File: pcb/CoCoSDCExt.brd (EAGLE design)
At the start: 101.6 x 47 mm, 49 parts, among them IC1 AM29F040J, IC10 YAC512-M, IC14 TL974, IC15 TL974, IC2 XC9572XLVQG64, IC3 AS6C4008SIN, IC9 YMF262-M, X1 EXPANSION_PORT_COCO, X2 EXPANSION_PORT_COCOS

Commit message: nearly routed
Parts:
- moved C20 12.3 mm to (23.2, 26.0)
- moved C2.2 11.9 mm to (16.5, 14.9), turned to 270 degrees
- moved JP1 7.62 mm to (-16.2, 19.7), turned to 270 degrees
- moved TCK 4.51 mm to (16.5, 19.4)
- moved TDI 4.24 mm to (14.6, 17.5)
- moved C2.4 3.17 mm to (17.5, 21.6)
- moved GND 2.73 mm to (14.6, 21.3)
- moved IC2 2.62 mm to (12.7, 18.4), turned to 45 degrees
- moved TMS 2.25 mm to (12.7, 19.4)
- moved C2.1 2.01 mm to (9.84, 21.9), turned to 90 degrees
- moved C2.3 1.71 mm to (9.84, 15.9), turned to 270 degrees
- moved TDO 1.62 mm to (12.7, 23.2)
- moved X2 1.27 mm to (0.00, 30.5)
- moved 3V3 0.45 mm to (10.8, 21.3)
- moved R16 0.32 mm to (47.3, 14.3)
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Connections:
- removed net !CE_SN: IC2.2
- removed net !CE_YM: IC2.58
- removed net !RESET_YM: IC2.59
- removed net !WE_SN: IC2.5
- removed net A0_YM: IC2.57
- removed net BD0: IC2.1
- removed net BD1: IC2.4
- removed net BD2: IC2.6
- removed net BD3: IC2.8
- removed net BD4: IC2.12
- removed net BD5: IC2.13
- removed net BD6: IC2.11
- removed net BD7: IC2.9
- removed net CH2: IC2.60
- removed net CLK_SN: IC2.10
- removed net CLK_YM: IC2.56
- removed net READY: IC2.7
- removed net VCC: IC3.32
- new net !CE_FLASH: IC1.22, IC2.2
- new net !CE_RAM: IC2.47, IC3.22
- net !CTS: now also IC2.20; no longer IC1.24
- net !RESET: now also IC2.4; no longer IC2.16
- net !SCS: now also IC2.23; no longer IC2.48
- net !SLENB: now also IC2.25; no longer IC2.50
- net !WE: now also IC2.51, IC3.29; no longer IC2.42
- net +5V: now also IC3.32
- net A0: now also IC2.5, IC3.5; no longer IC2.32
- net A1: now also IC2.1, IC3.6; no longer IC2.35
- net A10: now also IC2.49, IC3.31
- net A11: now also IC2.50, IC3.30
- net A12: now also IC2.17, IC3.4
- net A13: now also IC2.59, IC3.1; no longer IC2.33
- net A14: now also IC2.24; no longer IC2.49
- net A15: now also IC2.27; no longer IC2.34
- net A2: now also IC2.64, IC3.7; no longer IC2.38
- net A3: now also IC2.63, IC3.8; no longer IC2.40
- net A4: now also IC2.62, IC3.9; no longer IC2.43
- net A5: now also IC2.61, IC3.10; no longer IC2.45
- net A6: now also IC2.60, IC3.11
- net A7: now also IC2.58, IC3.12
- net A8: now also IC2.18, IC3.27
- net A9: now also IC2.52, IC3.28
- net BA14: now also IC2.57, IC3.26; no longer IC2.36
- net BA15: now also IC2.19, IC3.3; no longer IC2.47
- net BA16: now also IC2.22, IC3.2; no longer IC2.46
- net BA17: now also IC2.56, IC3.25; no longer IC2.39
- net BA18: now also IC2.48, IC3.23; no longer IC2.44
- net D0: now also IC2.13, IC3.17; no longer IC2.18
- net D1: now also IC2.12, IC3.15; no longer IC2.19
- net D2: now also IC2.11, IC3.18; no longer IC2.20
- net D3: now also IC2.10, IC3.14; no longer IC2.22
- net D4: now also IC2.9, IC3.19; no longer IC2.23
- net D5: now also IC2.8, IC3.13; no longer IC2.24
- net D6: now also IC2.7, IC3.20; no longer IC2.25
- net D7: now also IC2.6, IC3.21; no longer IC2.27
- net E: now also IC2.15; no longer IC2.17
- net GND: now also IC1.24, IC3.24; no longer IC1.22
- net R/!W: now also IC2.16; no longer IC2.31
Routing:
- net BA15: track 0.00 -> 93.9 mm, vias 0 -> 4
- net BA16: track 0.00 -> 92.9 mm, vias 0 -> 4
- net A0: track 25.0 -> 112.1 mm, vias 2 -> 5
- net A1: track 24.4 -> 110.8 mm, vias 0 -> 3
- net A13: track 25.5 -> 110.6 mm, vias 2 -> 5
- net D5: track 25.0 -> 109.5 mm, vias 2 -> 6
- net A12: track 25.0 -> 109.5 mm, vias 2 -> 5
- net A2: track 25.0 -> 106.9 mm, vias 2 -> 5
- net A3: track 24.4 -> 105.8 mm, vias 0 -> 3
- net A4: track 25.0 -> 104.8 mm, vias 2 -> 5
- net A5: track 24.4 -> 103.4 mm, vias 0 -> 3
- net A6: track 25.0 -> 103.8 mm, vias 2 -> 5
- net A7: track 24.4 -> 102.3 mm, vias 0 -> 3
- net D6: track 24.4 -> 96.1 mm, vias 0 -> 3
- net A8: track 25.0 -> 91.4 mm, vias 2 -> 6
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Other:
- board size 101.6 x 47 mm -> 101.6 x 47.3 mm

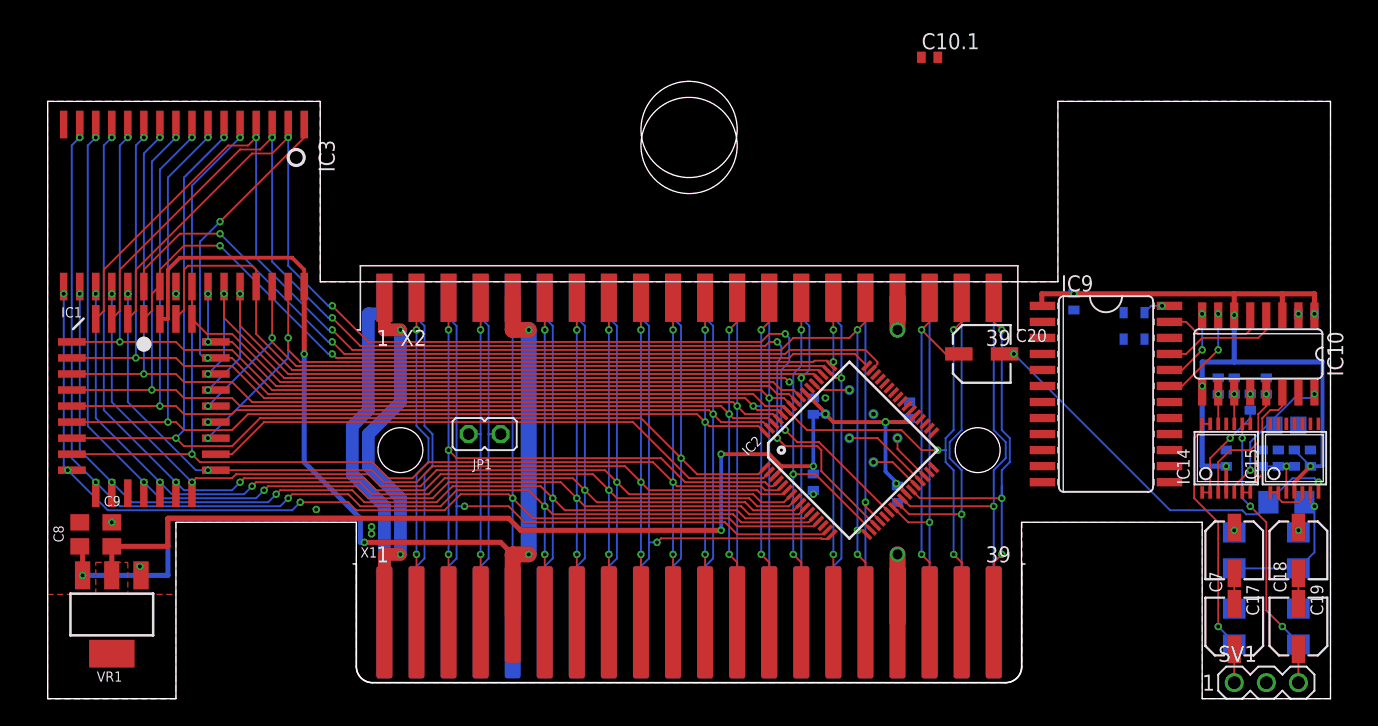
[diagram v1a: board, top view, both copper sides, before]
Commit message: fully routed
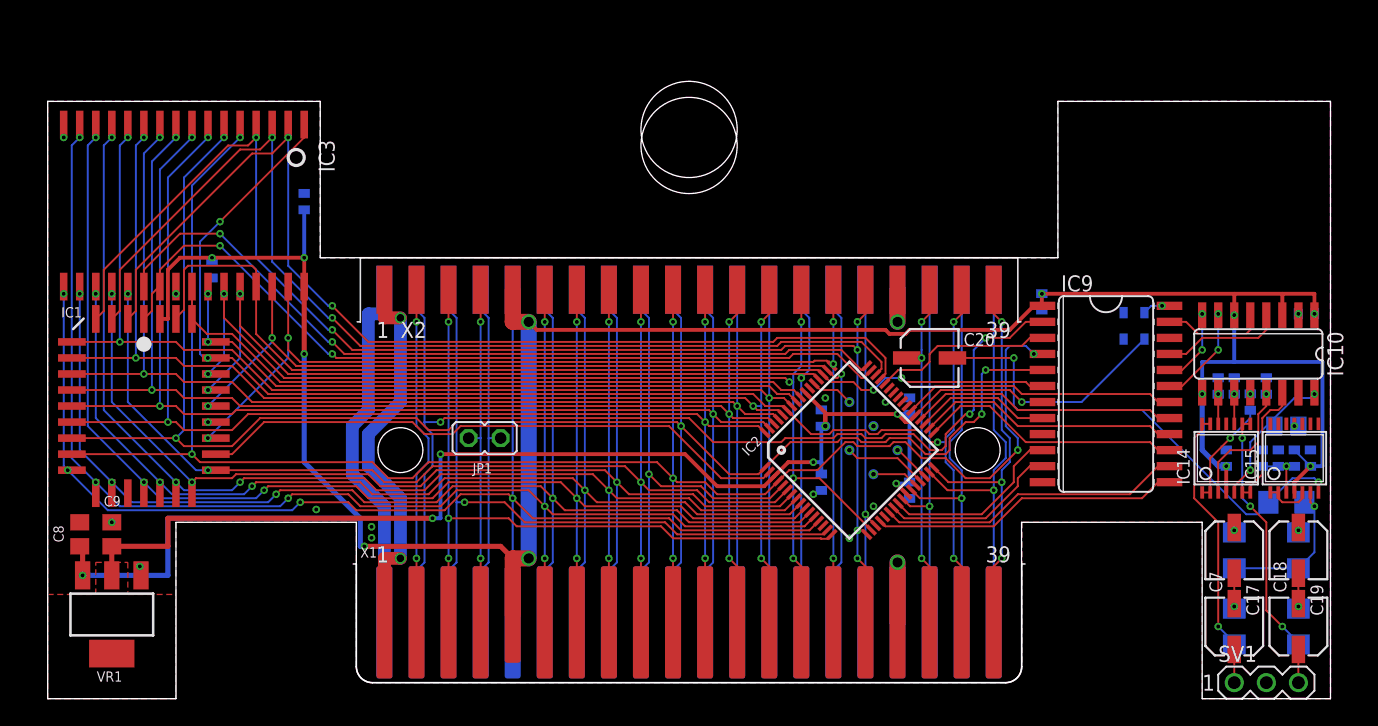
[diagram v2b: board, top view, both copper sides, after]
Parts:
- added C3.1: .1, resistor:C0402
- moved C1.1 86.7 mm to (-37.8, 32.7), turned to 270 degrees
- moved C10.1 36.1 mm to (48.9, 29.2), flipped to the bottom
- moved C20 4.14 mm to (19.1, 25.7)
- moved C9.1 2.54 mm to (27.9, 30.2)
- moved C2.1 1.14 mm to (10.5, 21.0)
- moved C2.2 1.00 mm to (17.5, 15.2)
- moved 3V3 0.95 mm to (10.8, 20.3)
- moved GND 0.95 mm to (14.6, 20.3)
- moved TCK 0.95 mm to (16.5, 18.4)
- moved TMS 0.95 mm to (12.7, 18.4)
- moved TDI 0.95 mm to (14.6, 16.5)
- moved TDO 0.95 mm to (12.7, 22.2)
- moved C2.3 0.63 mm to (10.5, 15.9)
- moved X2 0.63 mm to (0.00, 31.1)
- moved C2.4 0.32 mm to (17.5, 21.9)
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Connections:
- removed net !IRQ_AUDIO: IC9.2
- removed net !OE: IC9.7
- removed net AB0: IC9.4
- removed net AB1: IC9.5
- net !CE_RAM: now also IC2.48; no longer IC2.47
- net !CE_YMF262: now also IC2.35
- net !CTS: now also IC2.19; no longer IC2.20
- net !NMI: now also IC9.2
- net !RESET: now also IC2.16; no longer IC2.4
- net !RESET_AUDIO: now also IC2.44
- net !SCS: now also IC2.25; no longer IC2.23
- net !SLENB: now also IC2.31; no longer IC2.25
- net +5V: now also C3.1.1
- net A0: now also IC2.4, IC9.4; no longer IC2.5
- net A1: now also IC9.5
- net A14: now also IC2.27; no longer IC2.24
- net A15: now also IC2.32; no longer IC2.27
- net BA15: now also IC2.46; no longer IC2.19
- net BA16: now also IC2.45; no longer IC2.22
- net BA18: now also IC2.47; no longer IC2.48
- net DB0: now also IC2.24
- net DB1: now also IC2.23
- net DB2: now also IC2.20
- net DB3: now also IC2.22
- net DB4: now also IC2.33
- net DB5: now also IC2.34
- net DB6: now also IC2.36
- net DB7: now also IC2.38
- net GND: now also C3.1.2, IC9.7
- net R/!W: now also IC2.5; no longer IC2.16
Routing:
- net !NMI: track 26.8 -> 85.9 mm, vias 0 -> 3
- net +5V: track 176.9 -> 223.3 mm, vias 11 -> 13
- net A0: track 112.1 -> 147.0 mm, vias 5 -> 7
- net A1: track 110.8 -> 140.8 mm, vias 3 -> 5
- net DB2: track 0.00 -> 24.5 mm
- net DB3: track 0.00 -> 24.4 mm
- net DB7: track 0.00 -> 21.8 mm
- net DB6: track 0.00 -> 21.3 mm
- net +3V3: track 92.5 -> 113.8 mm, vias 6 -> 7
- net DB4: track 0.00 -> 21.0 mm
- net DB5: track 0.00 -> 20.9 mm
- net !WE: track 63.2 -> 81.7 mm, vias 0 -> 2
- net DB0: track 0.00 -> 14.6 mm
- net !RESET_AUDIO: track 0.00 -> 14.4 mm
- net DB1: track 0.00 -> 14.2 mm
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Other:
- outline, holes or cut-outs redrawn

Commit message: Added SN76489AN
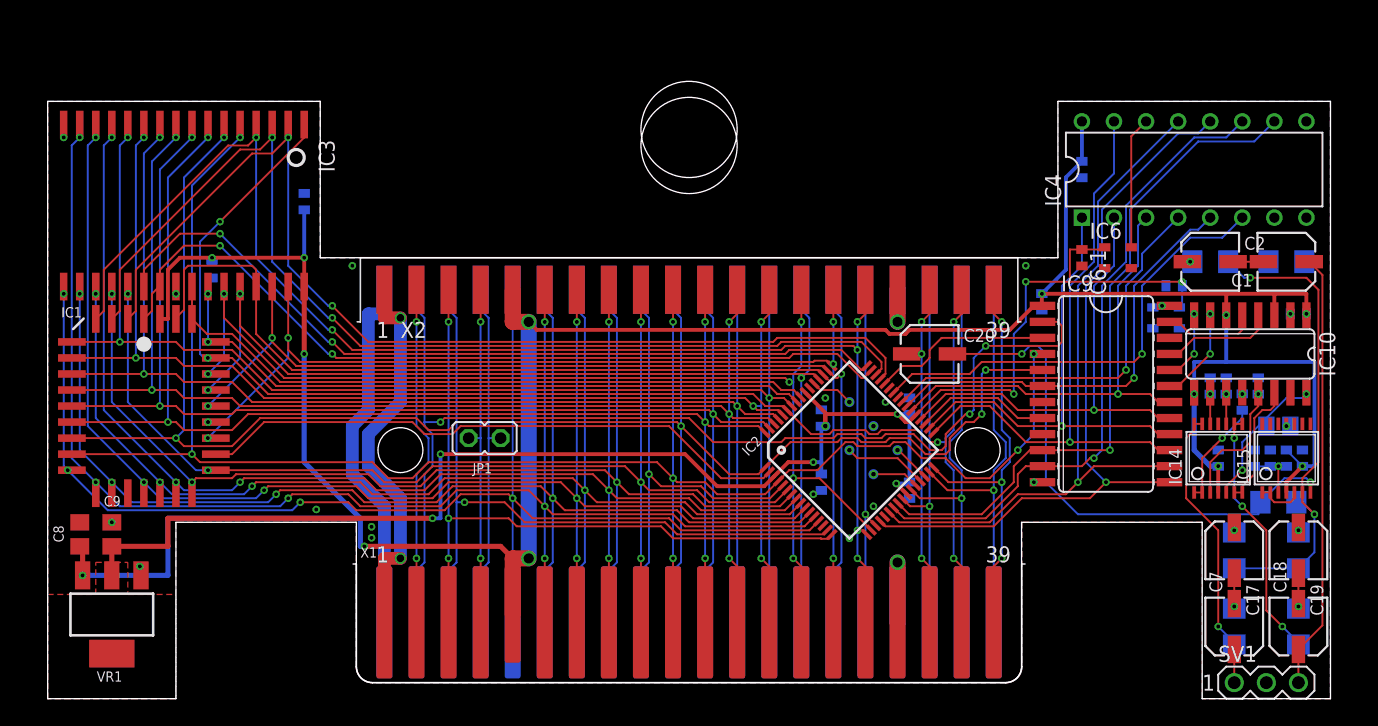
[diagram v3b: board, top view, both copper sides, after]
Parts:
- removed OSC1: 16MHz, crystal:ASE
- added C1, C2: 1u, cap-pan40:SV-B
- added C4.1: .1, rcl:C0402
- added C5.1, C6.1: .1, resistor:C0402
- added IC4: SN76489R, texas-instruments:DIL16-RP
- added IC5, IC6: 16MHz, crystal:ASE
- added R1: 2K, resistor:R1206
- added R2: 10K, resistor:R1206
- moved C10.1 0.64 mm to (48.3, 29.2)
- moved C15.1 0.64 mm to (41.9, 17.8)
- moved IC14 0.64 mm to (41.9, 17.8)
- moved IC15 0.64 mm to (47.3, 17.8)
- moved R14 0.64 mm to (47.3, 17.8)
- moved R15 0.64 mm to (44.8, 17.8)
- moved R9 0.64 mm to (43.8, 22.2)
- moved C14.1 0.63 mm to (48.6, 17.8)
- moved C15.2 0.63 mm to (46.0, 17.8)
- moved C4.2 0.63 mm to (46.7, 20.3)
- moved C4.4 0.63 mm to (45.1, 23.5)
- moved C4.5 0.63 mm to (42.5, 23.5)
- moved C4.6 0.63 mm to (41.3, 23.5)
- moved IC10 0.63 mm to (44.5, 26.0)
- moved R16 0.63 mm to (46.7, 14.3)
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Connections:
- new net !CE_SN: IC2.42, IC4.6
- new net !WE_AUDIO: IC2.39, IC4.5, IC9.6
- new net CN_CH_0: IC4.7
- new net N$1: IC4.14, IC6.3
- new net N$2: C1.-, C2.-, R1.1
- new net N$3: C2.+, R2.2
- new net READY: IC2.40, IC4.4
- new net SN_CH_0: R1.2
- net !WE: no longer IC9.6
- net +3V3: now also C5.1.1, C6.1.1, IC5.4, IC6.4; no longer OSC1.4
- net +5V: now also C4.1.1, IC4.16
- net AUDIO_R: now also C1.+
- net DB0: now also IC4.10
- net DB1: now also IC4.11
- net DB2: now also IC4.12
- net DB3: now also IC4.13
- net DB4: now also IC4.15
- net DB5: now also IC4.1
- net DB6: now also IC4.2
- net DB7: now also IC4.3
- net GND: now also C4.1.2, C5.1.2, C6.1.2, IC4.8, IC5.2, IC6.2; no longer OSC1.2
- net N$12: now also IC5.3; no longer OSC1.3
- net N$17: now also R2.1
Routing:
- net DB0: track 14.6 -> 54.0 mm, vias 0 -> 1
- net DB1: track 14.2 -> 51.8 mm, vias 0 -> 1
- net !CE_SN: track 0.00 -> 36.5 mm, vias 0 -> 1
- net !WE_AUDIO: track 0.00 -> 34.7 mm, vias 0 -> 1
- net DB2: track 24.5 -> 58.8 mm, vias 0 -> 1
- net DB3: track 24.4 -> 57.1 mm, vias 0 -> 1
- net READY: track 0.00 -> 32.5 mm, vias 0 -> 1
- net AUDIO_R: track 2.63 -> 34.6 mm
- net DB4: track 21.0 -> 47.8 mm, vias 0 -> 1
- net N$17: track 12.9 -> 38.7 mm, vias 1 -> 2
- net !WE: track 81.7 -> 64.0 mm, vias 2 -> 0
- net DB5: track 20.9 -> 38.1 mm, vias 0 -> 1
- net DB6: track 21.3 -> 38.2 mm, vias 0 -> 1
- net +3V3: track 113.8 -> 130.6 mm, vias 7 -> 9
- net DB7: track 21.8 -> 36.7 mm, vias 0 -> 1
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
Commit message: More fixes
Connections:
- removed net CN_CH_0: IC4.7
- new net N$4: IC2.43
- net SN_CH_0: now also IC4.7
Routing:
- net N$2: track 2.41 -> 2.80 mm, vias 0 -> 1
- net GND: vias 21 -> 26
- net +3V3: vias 9 -> 43
- added copper zone on layer 16, net +3V3
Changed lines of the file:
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@@
 <via x="26.67" y="33.02" extent="1-16" drill="0.3048"/>
 <via x="-26.67" y="33.02" extent="1-16" drill="0.3048"/>
-<wire x1="17.4625" y1="14.59" x2="27.305" y2="15.875" width="0" layer="19" extent="16-16"/>
+<via x="50.165" y="-0.635" extent="1-16" drill="0.3556"/>
+<via x="41.275" y="-0.635" extent="1-16" drill="0.3556"/>
+<via x="50.165" y="45.4025" extent="1-16" drill="0.3556"/>
+<via x="29.845" y="45.4025" extent="1-16" drill="0.3556"/>
+<via x="25.7175" y="12.7" extent="1-16" drill="0.3048"/>
 </signal>
 <signal name="-12V">
@@
 <wire x1="39.0525" y1="31.75" x2="39.0525" y2="29.9375" width="0.1524" layer="16"/>
 <wire x1="39.0525" y1="29.9375" x2="38.8325" y2="29.7175" width="0.1524" layer="16"/>
+<via x="-50.165" y="6.6675" extent="1-16" drill="0.3048"/>
+<via x="-49.2125" y="6.6675" extent="1-16" drill="0.3048"/>
+<via x="-48.26" y="6.6675" extent="1-16" drill="0.3048"/>
+<via x="-47.3075" y="6.6675" extent="1-16" drill="0.3048"/>
+<via x="-46.355" y="6.6675" extent="1-16" drill="0.3048"/>
+<via x="-45.72" y="6.6675" extent="1-16" drill="0.3048"/>
+<via x="-45.085" y="6.6675" extent="1-16" drill="0.3048"/>
+<via x="-44.1325" y="6.6675" extent="1-16" drill="0.3048"/>
+<via x="-43.18" y="6.6675" extent="1-16" drill="0.3048"/>
+<via x="-42.2275" y="6.6675" extent="1-16" drill="0.3048"/>
+<via x="-41.275" y="6.6675" extent="1-16" drill="0.3048"/>
+<via x="-41.275" y="5.715" extent="1-16" drill="0.3048"/>
+<via x="-41.275" y="4.7625" extent="1-16" drill="0.3048"/>
+<via x="-41.275" y="3.81" extent="1-16" drill="0.3048"/>
+<via x="-41.275" y="2.8575" extent="1-16" drill="0.3048"/>
+<via x="-41.275" y="1.905" extent="1-16" drill="0.3048"/>
+<via x="-41.275" y="0.9525" extent="1-16" drill="0.3048"/>
+<via x="-41.275" y="0" extent="1-16" drill="0.3048"/>
+<via x="-41.91" y="-0.635" extent="1-16" drill="0.3048"/>
+<via x="-42.8625" y="-0.635" extent="1-16" drill="0.3048"/>
+<via x="-43.815" y="-0.635" extent="1-16" drill="0.3048"/>
+<via x="-44.7675" y="-0.635" extent="1-16" drill="0.3048"/>
+<via x="-45.72" y="-0.635" extent="1-16" drill="0.3048"/>
+<via x="-46.6725" y="-0.635" extent="1-16" drill="0.3048"/>
+<via x="-47.625" y="-0.635" extent="1-16" drill="0.3048"/>
+<via x="-48.5775" y="-0.635" extent="1-16" drill="0.3048"/>
+<via x="-49.53" y="-0.635" extent="1-16" drill="0.3048"/>
+<via x="-50.165" y="0" extent="1-16" drill="0.3048"/>
+<via x="-50.165" y="0.9525" extent="1-16" drill="0.3048"/>
+<via x="-50.165" y="1.905" extent="1-16" drill="0.3048"/>
+<via x="-50.165" y="2.8575" extent="1-16" drill="0.3048"/>
+<via x="-50.165" y="3.81" extent="1-16" drill="0.3048"/>
+<via x="-50.165" y="4.7625" extent="1-16" drill="0.3048"/>
+<via x="-50.165" y="5.715" extent="1-16" drill="0.3048"/>
+<polygon width="0.1524" layer="16">
+<vertex x="-50.8" y="6.985"/>
+<vertex x="-50.8" y="-1.27"/>
+<vertex x="-40.64" y="-1.27"/>
+<vertex x="-40.64" y="6.985"/>
+</polygon>
 </signal>
 <signal name="R/!W">
@@
 <wire x1="35.0225" y1="43.2775" x2="36.195" y2="44.45" width="0.1524" layer="1"/>
 </signal>
-<signal name="CN_CH_0">
-<contactref element="IC4" pad="7"/>
-</signal>
 <signal name="N$2">
 <contactref element="R1" pad="1"/>
@@
 <contactref element="C2" pad="-"/>
 <wire x1="43.085" y1="33.3375" x2="45.4975" y2="33.3375" width="0.1524" layer="1"/>
-<wire x1="45.4975" y1="33.3375" x2="45.8855" y2="33.3375" width="0" layer="19" extent="1-16"/>
+<wire x1="45.4975" y1="33.3375" x2="45.72" y2="33.3375" width="0.1524" layer="1"/>
+<via x="45.72" y="33.3375" extent="1-16" drill="0.3048"/>
+<wire x1="45.72" y1="33.3375" x2="45.8855" y2="33.3375" width="0.1524" layer="16"/>
 </signal>
 <signal name="N$3">
@@
 <signal name="SN_CH_0">
 <contactref element="R1" pad="2"/>
+<contactref element="IC4" pad="7"/>
+<wire x1="46.355" y1="36.83" x2="48.7295" y2="33.3375" width="0" layer="19" extent="16-16"/>
+</signal>
+<signal name="N$4">
+<contactref element="IC2" pad="43"/>
 </signal>
 </signals>
